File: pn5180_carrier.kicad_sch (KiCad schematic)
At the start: 35 parts, among them J1 Bay 0 (CLIK-Mate 2x5), J10 24V IN (CLIK-Mate 1x2), J2 Bay 1 (CLIK-Mate 2x5), J3 Bay 2 (CLIK-Mate 2x5), J4 Bay 3 (CLIK-Mate 2x5), J5 Bay 4 (CLIK-Mate 2x5), J6 Bay 5 (CLIK-Mate 2x5), J7 Bay 6 (CLIK-Mate 2x5), J8 Bay 7 (CLIK-Mate 2x5), U1 74HC138, U2 74HC151, U4 TLV1117LV33DCYR, U5 XIAO ESP32C6, U6 MP1584EN module (set 5.0V)

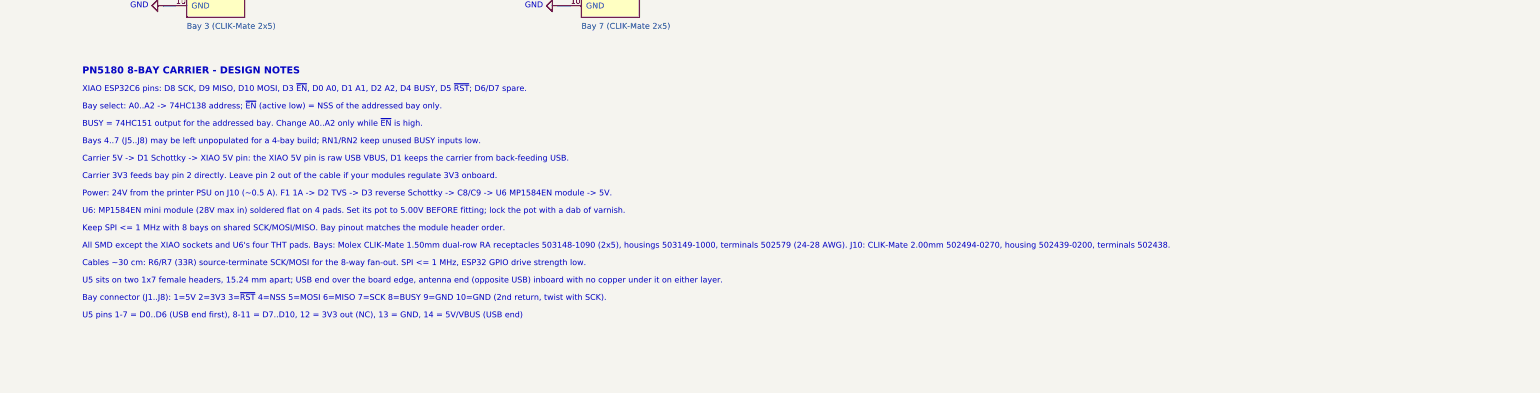
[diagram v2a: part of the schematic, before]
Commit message: Schematic DESIGN NOTES: terse one-line notes that fit the A3 frame; re-export renders
Netlist (38 nets, 189 nodes, 0 problems) and ERC unchanged.

Co-Authored-By: Claude Fable 5.1 <noreply@anthropic.com>
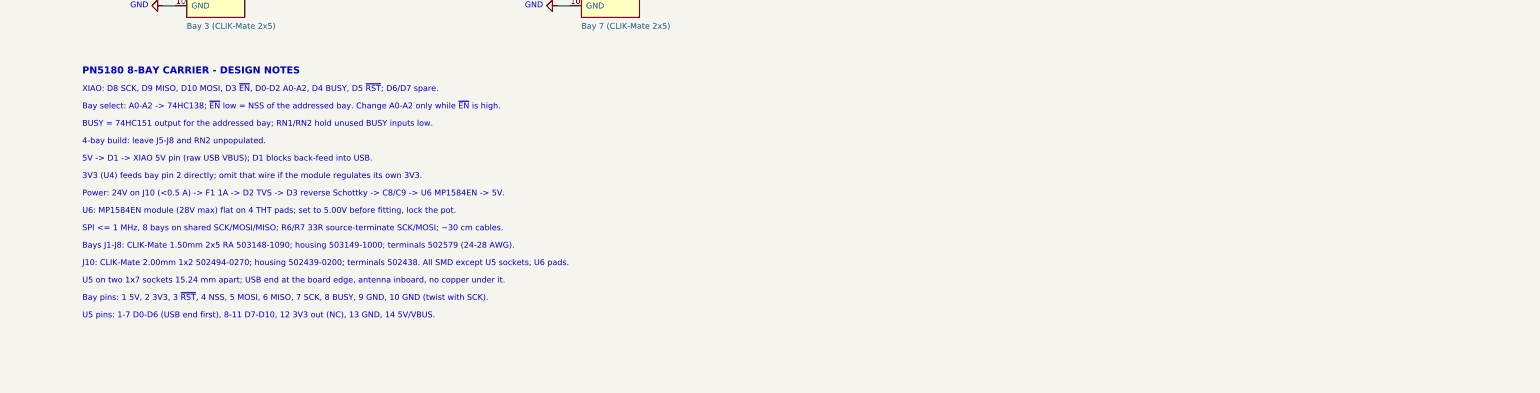
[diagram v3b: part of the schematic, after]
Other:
- note added: "3V3 (U4) feeds bay pin 2 directly; omit that wire if the module regulates its own 3V3."
- note added: "4-bay build: leave J5-J8 and RN2 unpopulated."
- note added: "5V -> D1 -> XIAO 5V pin (raw USB VBUS); D1 blocks back-feed into USB."
- note added: "BUSY = 74HC151 output for the addressed bay; RN1/RN2 hold unused BUSY inputs low."
- note added: "Bay pins: 1 5V, 2 3V3, 3 ~{RST}, 4 NSS, 5 MOSI, 6 MISO, 7 SCK, 8 BUSY, 9 GND, 10 GND (twist with SCK)."
- note added: "Bay select: A0-A2 -> 74HC138; ~{EN} low = NSS of the addressed bay. Change A0-A2 only while ~{EN} is high."
- note added: "Bays J1-J8: CLIK-Mate 1.50mm 2x5 RA 503148-1090; housing 503149-1000; terminals 502579 (24-28 AWG)."
- note added: "J10: CLIK-Mate 2.00mm 1x2 502494-0270; housing 502439-0200; terminals 502438. All SMD except U5 sockets, U6 pads."
- note added: "Power: 24V on J10 (<0.5 A) -> F1 1A -> D2 TVS -> D3 reverse Schottky -> C8/C9 -> U6 MP1584EN -> 5V."
- note added: "SPI <= 1 MHz, 8 bays on shared SCK/MOSI/MISO; R6/R7 33R source-terminate SCK/MOSI; ~30 cm cables."
- note added: "U5 on two 1x7 sockets 15.24 mm apart; USB end at the board edge, antenna inboard, no copper under it."
- note added: "U5 pins: 1-7 D0-D6 (USB end first), 8-11 D7-D10, 12 3V3 out (NC), 13 GND, 14 5V/VBUS."
- note added: "U6: MP1584EN module (28V max) flat on 4 THT pads; set to 5.00V before fitting, lock the pot."
- note added: "XIAO: D8 SCK, D9 MISO, D10 MOSI, D3 ~{EN}, D0-D2 A0-A2, D4 BUSY, D5 ~{RST}; D6/D7 spare."
- note removed: "All SMD except the XIAO sockets and U6's four THT pads. Bays: Molex CLIK-Mate 1.50mm dual-row RA receptacles 503148-1090 (2x5), housings 503149-1000, terminals 502579 (24-28 AWG). J10: CLIK-Mate 2.00mm 502494-0270, housing 502439-0200, terminals 502438."
- note removed: "BUSY = 74HC151 output for the addressed bay. Change A0..A2 only while ~{EN} is high."
- note removed: "Bay connector (J1..J8): 1=5V 2=3V3 3=~{RST} 4=NSS 5=MOSI 6=MISO 7=SCK 8=BUSY 9=GND 10=GND (2nd return, twist with SCK)."
- note removed: "Bay select: A0..A2 -> 74HC138 address; ~{EN} (active low) = NSS of the addressed bay only."
- note removed: "Bays 4..7 (J5..J8) may be left unpopulated for a 4-bay build; RN1/RN2 keep unused BUSY inputs low."
- note removed: "Cables ~30 cm: R6/R7 (33R) source-terminate SCK/MOSI for the 8-way fan-out. SPI <= 1 MHz, ESP32 GPIO drive strength low."
- note removed: "Carrier 3V3 feeds bay pin 2 directly. Leave pin 2 out of the cable if your modules regulate 3V3 onboard."
- note removed: "Carrier 5V -> D1 Schottky -> XIAO 5V pin: the XIAO 5V pin is raw USB VBUS, D1 keeps the carrier from back-feeding USB."
- note removed: "Keep SPI <= 1 MHz with 8 bays on shared SCK/MOSI/MISO. Bay pinout matches the module header order."
- note removed: "Power: 24V from the printer PSU on J10 (~0.5 A). F1 1A -> D2 TVS -> D3 reverse Schottky -> C8/C9 -> U6 MP1584EN module -> 5V."
- note removed: "U5 pins 1-7 = D0..D6 (USB end first), 8-11 = D7..D10, 12 = 3V3 out (NC), 13 = GND, 14 = 5V/VBUS (USB end)"
- note removed: "U5 sits on two 1x7 female headers, 15.24 mm apart; USB end over the board edge, antenna end (opposite USB) inboard with no copper under it on either layer."
- note removed: "U6: MP1584EN mini module (28V max in) soldered flat on 4 pads. Set its pot to 5.00V BEFORE fitting; lock the pot with a dab of varnish."
- note removed: "XIAO ESP32C6 pins: D8 SCK, D9 MISO, D10 MOSI, D3 ~{EN}, D0 A0, D1 A1, D2 A2, D4 BUSY, D5 ~{RST}; D6/D7 spare."
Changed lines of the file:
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@@
 		(comment 2 "Originally generated with gen_kicad.py; hand-edited in KiCad 10 since rev 1.3")
 	)
-	(text "U5 sits on two 1x7 female headers, 15.24 mm apart; USB end over the board edge, antenna end (opposite USB) inboard with no copper under it on either layer."
+	(text "U5 on two 1x7 sockets 15.24 mm apart; USB end at the board edge, antenna inboard, no copper under it."
 		(exclude_from_sim no)
 		(at 243.84 233.68 0)
@@
 		)
 	)
-	(text "Bays 4..7 (J5..J8) may be left unpopulated for a 4-bay build; RN1/RN2 keep unused BUSY inputs low."
+	(text "4-bay build: leave J5-J8 and RN2 unpopulated."
 		(exclude_from_sim no)
 		(at 243.84 203.2 0)
@@
 		)
 	)
-	(text "XIAO ESP32C6 pins: D8 SCK, D9 MISO, D10 MOSI, D3 ~{EN}, D0 A0, D1 A1, D2 A2, D4 BUSY, D5 ~{RST}; D6/D7 spare."
+	(text "XIAO: D8 SCK, D9 MISO, D10 MOSI, D3 ~{EN}, D0-D2 A0-A2, D4 BUSY, D5 ~{RST}; D6/D7 spare."
 		(exclude_from_sim no)
 		(at 243.84 191.77 0)
@@
 		)
 	)
-	(text "Keep SPI <= 1 MHz with 8 bays on shared SCK/MOSI/MISO. Bay pinout matches the module header order."
+	(text "SPI <= 1 MHz, 8 bays on shared SCK/MOSI/MISO; R6/R7 33R source-terminate SCK/MOSI; ~30 cm cables."
 		(exclude_from_sim no)
 		(at 243.84 222.25 0)
@@
 		)
 	)
-	(text "Carrier 5V -> D1 Schottky -> XIAO 5V pin: the XIAO 5V pin is raw USB VBUS, D1 keeps the carrier from back-feeding USB."
+	(text "5V -> D1 -> XIAO 5V pin (raw USB VBUS); D1 blocks back-feed into USB."
 		(exclude_from_sim no)
 		(at 243.84 207.01 0)
@@
 		)
 	)
-	(text "U6: MP1584EN mini module (28V max in) soldered flat on 4 pads. Set its pot to 5.00V BEFORE fitting; lock the pot with a dab of varnish."
+	(text "U6: MP1584EN module (28V max) flat on 4 THT pads; set to 5.00V before fitting, lock the pot."
 		(exclude_from_sim no)
 		(at 243.84 218.44 0)
@@
 		)
 	)
-	(text "Bay select: A0..A2 -> 74HC138 address; ~{EN} (active low) = NSS of the addressed bay only."
+	(text "Bay select: A0-A2 -> 74HC138; ~{EN} low = NSS of the addressed bay. Change A0-A2 only while ~{EN} is high."
 		(exclude_from_sim no)
 		(at 243.84 195.58 0)
@@
 		)
 	)
-	(text "Bay connector (J1..J8): 1=5V 2=3V3 3=~{RST} 4=NSS 5=MOSI 6=MISO 7=SCK 8=BUSY 9=GND 10=GND (2nd return, twist with SCK)."
+	(text "Bay pins: 1 5V, 2 3V3, 3 ~{RST}, 4 NSS, 5 MOSI, 6 MISO, 7 SCK, 8 BUSY, 9 GND, 10 GND (twist with SCK)."
 		(exclude_from_sim no)
 		(at 243.84 237.49 0)
@@
 		)
 	)
-	(text "BUSY = 74HC151 output for the addressed bay. Change A0..A2 only while ~{EN} is high."
+	(text "BUSY = 74HC151 output for the addressed bay; RN1/RN2 hold unused BUSY inputs low."
 		(exclude_from_sim no)
 		(at 243.84 199.39 0)
@@
 		)
 	)
-	(text "U5 pins 1-7 = D0..D6 (USB end first), 8-11 = D7..D10, 12 = 3V3 out (NC), 13 = GND, 14 = 5V/VBUS (USB end)"
+	(text "U5 pins: 1-7 D0-D6 (USB end first), 8-11 D7-D10, 12 3V3 out (NC), 13 GND, 14 5V/VBUS."
 		(exclude_from_sim no)
 		(at 243.84 241.3 0)
@@
 		)
 	)
-	(text "Power: 24V from the printer PSU on J10 (~0.5 A). F1 1A -> D2 TVS -> D3 reverse Schottky -> C8/C9 -> U6 MP1584EN module -> 5V."
+	(text "Power: 24V on J10 (<0.5 A) -> F1 1A -> D2 TVS -> D3 reverse Schottky -> C8/C9 -> U6 MP1584EN -> 5V."
 		(exclude_from_sim no)
 		(at 243.84 214.63 0)
@@
 		)
 	)
-	(text "All SMD except the XIAO sockets and U6's four THT pads. Bays: Molex CLIK-Mate 1.50mm dual-row RA receptacles 503148-1090 (2x5), housings 503149-1000, terminals 502579 (24-28 AWG). J10: CLIK-Mate 2.00mm 502494-0270, housing 502439-0200, terminals 502438."
+	(text "Bays J1-J8: CLIK-Mate 1.50mm 2x5 RA 503148-1090; housing 503149-1000; terminals 502579 (24-28 AWG)."
 		(exclude_from_sim no)
 		(at 243.84 226.06 0)
@@
 		)
 	)
-	(text "Carrier 3V3 feeds bay pin 2 directly. Leave pin 2 out of the cable if your modules regulate 3V3 onboard."
+	(text "3V3 (U4) feeds bay pin 2 directly; omit that wire if the module regulates its own 3V3."
 		(exclude_from_sim no)
 		(at 243.84 210.82 0)
@@
 		)
 	)
-	(text "Cables ~30 cm: R6/R7 (33R) source-terminate SCK/MOSI for the 8-way fan-out. SPI <= 1 MHz, ESP32 GPIO drive strength low."
+	(text "J10: CLIK-Mate 2.00mm 1x2 502494-0270; housing 502439-0200; terminals 502438. All SMD except U5 sockets, U6 pads."
 		(exclude_from_sim no)
 		(at 243.84 229.87 0)

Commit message: 3D models for the parts KiCad ships none for; preview render and tools
- carrier.3dshapes/: simplified VRML models generated by tools/gen_3d_models.py —
  CLIK-Mate 503148-1090 2x5 and 502494-0270 1x2 receptacles, XIAO ESP32C6 on its two
  8.5 mm sockets (rounded board, castellations, USB-C, shield, u.FL, chip antenna,
  buttons), MP1584EN module, Littelfuse NANO2 fuse
- carrier.pretty: model references on the three custom footprints; project-local
  copies of the stock J10 and F1 footprints that differ only in the model path;
  schematic/BOM/README point J10 and F1 at carrier:
- PCB: model references text-patched into the embedded footprints (all 35 resolve);
  otherwise identical to the owner's a606ea7 save
- tools/: footprint and model generators, render_3d_preview.py (kicad-cli pcb render on
  a temp copy); pn5180_carrier_3d_preview.png; renders/ ignored
- README/CLAUDE.md/MEMORY.md: files, tooling, conventions, PCB status, item 13

Co-Authored-By: Claude Fable 5.1 <noreply@anthropic.com>
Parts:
- F1: footprint Fuse:Fuse_Littelfuse-NANO2-451_453 -> carrier:Fuse_Littelfuse-NANO2-451_453
- J10: footprint Connector_Molex:Molex_CLIK-Mate_502494-0270_1x02-1MP_P2.00mm_Horizontal -> carrier:Molex_CLIK-Mate_502494-0270_1x02-1MP_P2.00mm_Horizontal
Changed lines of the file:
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@@
 			)
 		)
-		(property "Footprint" "Connector_Molex:Molex_CLIK-Mate_502494-0270_1x02-1MP_P2.00mm_Horizontal"
+		(property "Footprint" "carrier:Molex_CLIK-Mate_502494-0270_1x02-1MP_P2.00mm_Horizontal"
 			(at 20.32 35.56 0)
 			(hide yes)
@@
 			)
 		)
-		(property "Footprint" "Fuse:Fuse_Littelfuse-NANO2-451_453"
+		(property "Footprint" "carrier:Fuse_Littelfuse-NANO2-451_453"
 			(at 86.36 223.52 0)
 			(hide yes)

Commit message: XIAO soldered flat (castellated SMD footprint), photo-accurate XIAO and MP1584EN models
- carrier.pretty/Seeed_XIAO_ESP32C6_SMD (tools/gen_xiao_smd_fp.py): 14 pads 1.5x2.5 at
  2.54 mm on the module edges, same 1-14 numbering; U5 switched in the schematic, BOM
  and (by script, same position/nets/fields) on the PCB; the Wuerth sockets leave the
  Mouser order list. Tracks to U5 end 1.27 mm short of the new pads (re-route).
- 3D: XIAO rebuilt from the owner's photos (rounded board, half-hole castellations,
  USB-C over the edge, R/B buttons and LEDs, white shield, u.FL, chip antenna), flat and
  socketed variants; MP1584EN per the owner's photo (black PCB, shielded inductor,
  SOIC-8, ceramics, diode, plated corner holes, no trimmer); J10 on the stock F.Fab
  outline; fuse model.
- Docs: sockets removed everywhere, post-swap DRC numbers (zones saved unfilled: refill
  before quoting DRC), stock-footprint list now nine names, stale "PCB not yet updated"
  fixed, open items 12/14, fuse wording aligned between BOM CSV and README.

Co-Authored-By: Claude Fable 5.1 <noreply@anthropic.com>
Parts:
- U5: footprint carrier:Seeed_XIAO_2x7_Socket -> carrier:Seeed_XIAO_ESP32C6_SMD
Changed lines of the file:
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@@
 			)
 		)
-		(property "Footprint" "carrier:Seeed_XIAO_2x7_Socket"
+		(property "Footprint" "carrier:Seeed_XIAO_ESP32C6_SMD"
 			(at 50.8 101.6 0)
 			(hide yes)

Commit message: U6 is the fixed-5 V module: strip the pot-setting text; align U5/F1 fields
- U6: Value "MP1584EN module, fixed 5V", Description and library ki_description say
  fixed 5V output (no trimmer); DESIGN NOTES line, BOM CSV, README §buck and BOM row
  reworded; CLAUDE.md open item 9 resolved, MEMORY.md item 7 and open question closed.
- U5: MPN "XIAO ESP32C6" in the schematic to match the owner's shortened PCB silk
  field (SKU 113991182 moved into Description) — DRC parity back to 0; Description
  and the two DESIGN NOTES lines now say soldered flat on 14 castellations, no sockets.
- F1: Value "1A", Description "NANO2 451/453 (fast-acting series)" in schematic and PCB.
- Re-exported schematic PDF/PNG. Checks: netlist 38/189/0, ERC 82 (unchanged),
  DRC parity 0; refilled DRC on the owner's 12:15 save is 170/89 (logged in MEMORY.md).

Co-Authored-By: Claude Fable 5.1 <noreply@anthropic.com>
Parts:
- F1: value 1A slow -> 1A
- U5: MPN XIAO ESP32C6 (SKU 113991182) -> XIAO ESP32C6
- U6: value MP1584EN module (set 5.0V) -> MP1584EN module, fixed 5V
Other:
- note added: "J10: CLIK-Mate 2.00mm 1x2 502494-0270; housing 502439-0200; terminals 502438. All SMD except U6's 4 THT pads."
- note added: "U5 soldered flat on its 14 castellations; USB end at the board edge, antenna inboard, no copper under it."
- note added: "U6: MP1584EN module, fixed 5V output (no trimmer), 28V max in; flat on 4 THT pads."
- note removed: "J10: CLIK-Mate 2.00mm 1x2 502494-0270; housing 502439-0200; terminals 502438. All SMD except U5 sockets, U6 pads."
- note removed: "U5 on two 1x7 sockets 15.24 mm apart; USB end at the board edge, antenna inboard, no copper under it."
- note removed: "U6: MP1584EN module (28V max) flat on 4 THT pads; set to 5.00V before fitting, lock the pot."
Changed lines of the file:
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@@
 		(comment 2 "Originally generated with gen_kicad.py; hand-edited in KiCad 10 since rev 1.3")
 	)
-	(text "U5 on two 1x7 sockets 15.24 mm apart; USB end at the board edge, antenna inboard, no copper under it."
+	(text "U5 soldered flat on its 14 castellations; USB end at the board edge, antenna inboard, no copper under it."
 		(exclude_from_sim no)
 		(at 243.84 233.68 0)
@@
 		)
 	)
-	(text "U6: MP1584EN module (28V max) flat on 4 THT pads; set to 5.00V before fitting, lock the pot."
+	(text "U6: MP1584EN module, fixed 5V output (no trimmer), 28V max in; flat on 4 THT pads."
 		(exclude_from_sim no)
 		(at 243.84 218.44 0)
@@
 		)
 	)
-	(text "J10: CLIK-Mate 2.00mm 1x2 502494-0270; housing 502439-0200; terminals 502438. All SMD except U5 sockets, U6 pads."
+	(text "J10: CLIK-Mate 2.00mm 1x2 502494-0270; housing 502439-0200; terminals 502438. All SMD except U6's 4 THT pads."
 		(exclude_from_sim no)
 		(at 243.84 229.87 0)
@@
 			)
 		)
-		(property "Value" "MP1584EN module (set 5.0V)"
+		(property "Value" "MP1584EN module, fixed 5V"
 			(at 114.3 254 0)
 			(show_name no)
@@
 			)
 		)
-		(property "Description" "22x17mm adjustable module, user-supplied (Amazon); set to 5.0V"
+		(property "Description" "22x17mm fixed-5V module (no trimmer), user-supplied (Amazon)"
 			(at 132.08 246.38 0)
 			(hide yes)
@@
 			)
 		)
-		(property "Description" "XIAO ESP32C6 module, 2x7 pins on 15.24mm (user-supplied; verify Mouser #)"
+		(property "Description" "XIAO ESP32C6 module (Seeed SKU 113991182), soldered flat on its 14 castellations (user-supplied; verify Mouser #)"
 			(at 50.8 101.6 0)
 			(hide yes)
@@
 			)
 		)
-		(property "MPN" "XIAO ESP32C6 (SKU 113991182)"
+		(property "MPN" "XIAO ESP32C6"
 			(at 50.8 101.6 0)
 			(hide yes)
@@
 			)
 		)
-		(property "Value" "1A slow"
+		(property "Value" "1A"
 			(at 82.55 226.314 0)
 			(show_name no)
@@
 			)
 		)
-		(property "Description" "1A slow-blow SMD fuse, NANO2"
+		(property "Description" "1A SMD fuse, NANO2 451/453 (fast-acting series; see CLAUDE.md open item 13)"
 			(at 86.36 223.52 0)
 			(hide yes)
